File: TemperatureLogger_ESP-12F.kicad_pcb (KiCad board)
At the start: 2 copper layers, 43.7 x 43.7 mm, 19 parts, among them J1 Power for additional devices, J2 Additional I2C device, J3 Barrel_Jack, J4 FTDI, SW1 GND_to_reset, SW2 GND_to_program, U1 ESP-12F, U2 MCP1700-3302E, U6 GY-B11(BME-280)

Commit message: Fixing the programming switch and starting to change the DC jack to fit in the box (component still too high)
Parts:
- J4: value FTDI -> FTDI_Cable
- R7: value 330 -> 100
- SW2: footprint SamacSys_Parts:EG1218 -> TemperatureLogger_ESP-12F:EG1218
- U2: value MCP1700-3302E -> MCP1700-3302E_TO92
- U6: value GY-B11(BME-280) -> GY-B11(BMP-280)
- moved J3 5.51 mm to (142.8, 114.4)
- turned SW2 to 270 degrees
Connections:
- J3 pad 3: (no net) -> Net-(J3-Pad3)
- SW2 pad 2: Earth -> Net-(SW2-Pad2)
- SW2 pad 3: (no net) -> Earth
- U1 pad 10: (no net) -> Net-(U1-Pad10)
- U1 pad 11: (no net) -> Net-(U1-Pad11)
- U1 pad 12: (no net) -> Net-(U1-Pad12)
- U1 pad 13: (no net) -> Net-(U1-Pad13)
- U1 pad 18: Net-(R5-Pad2) -> Net-(SW2-Pad2)
- U1 pad 19: (no net) -> Net-(U1-Pad19)
- U1 pad 2: (no net) -> Net-(U1-Pad2)
- U1 pad 20: (no net) -> Net-(U1-Pad20)
- U1 pad 5: (no net) -> Net-(U1-Pad5)
- U1 pad 7: (no net) -> Net-(U1-Pad7)
- U1 pad 9: (no net) -> Net-(U1-Pad9)
- U6 pad 5: (no net) -> Net-(U6-Pad5)
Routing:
- net Net-(SW2-Pad2): track 0.00 -> 85.0 mm
- net Net-(R5-Pad2): track 87.7 -> 8.82 mm
- net /3.3V: track 160.9 -> 163.9 mm

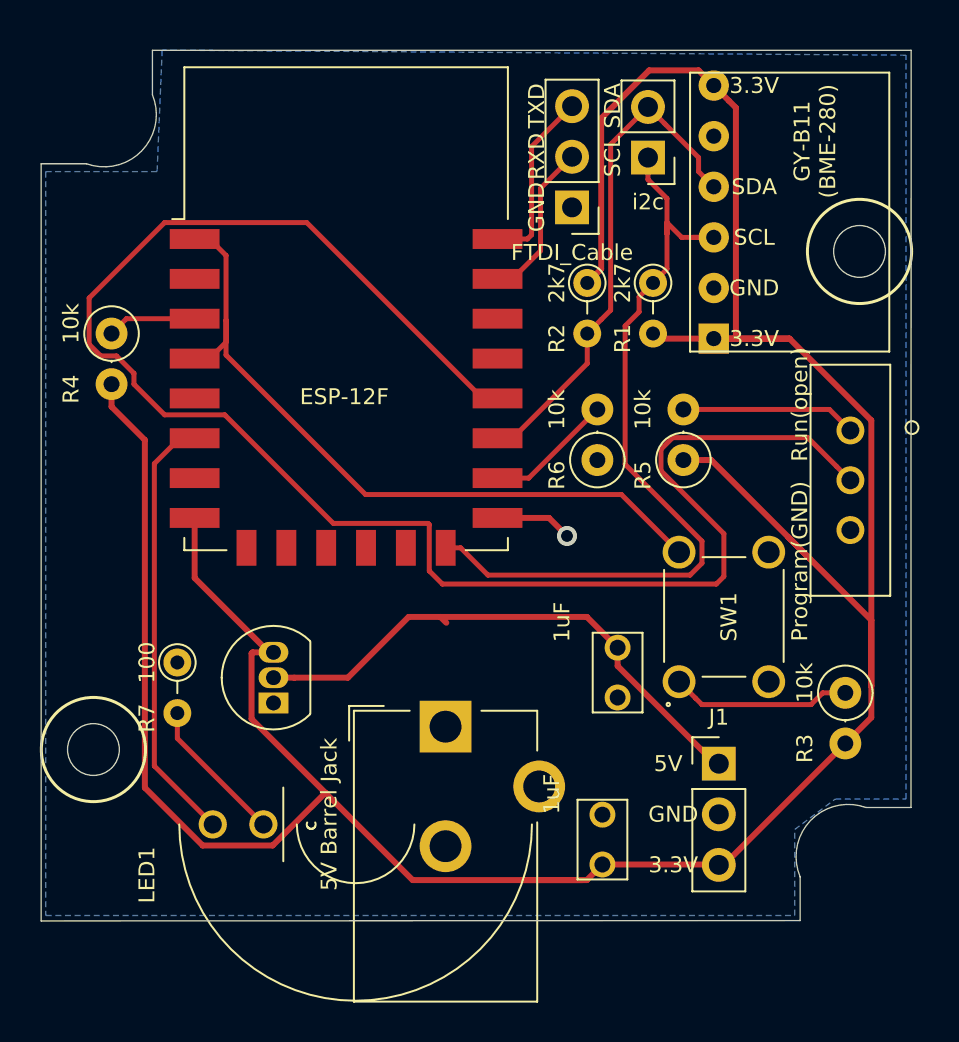
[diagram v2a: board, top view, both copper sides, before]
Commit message: New revisions with headers for power and external sensor
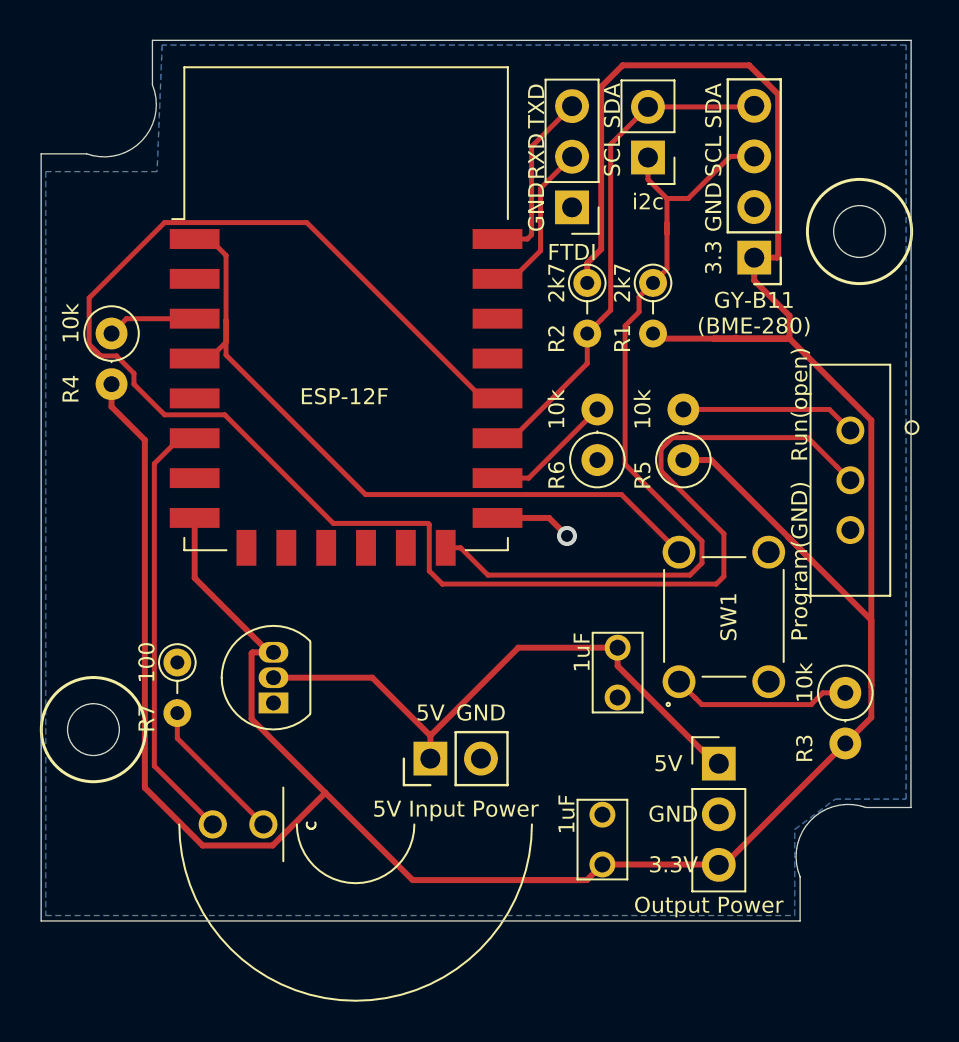
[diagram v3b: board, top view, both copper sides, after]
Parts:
- J3: footprint Connector_BarrelJack:BarrelJack_CUI_PJ-102AH_Horizontal -> Connector_PinHeader_2.54mm:PinHeader_1x02_P2.54mm_Vertical
- J4: value FTDI_Cable -> FTDI
- Output Power: renamed from J1
- U6: footprint ChickmaticPhase3-Simplify:GY-BME280-3.3 -> Connector_PinHeader_2.54mm:PinHeader_1x04_P2.54mm_Vertical
- moved U6 2.90 mm to (158.3, 90.8)
- moved J3 1.78 mm to (142.0, 116.0), turned to 90 degrees
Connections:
- U1 pad 10: Net-(U1-Pad10) -> (no net)
- U1 pad 11: Net-(U1-Pad11) -> (no net)
- U1 pad 12: Net-(U1-Pad12) -> (no net)
- U1 pad 13: Net-(U1-Pad13) -> (no net)
- U1 pad 19: Net-(U1-Pad19) -> (no net)
- U1 pad 2: Net-(U1-Pad2) -> (no net)
- U1 pad 20: Net-(U1-Pad20) -> (no net)
- U1 pad 5: Net-(U1-Pad5) -> (no net)
- U1 pad 7: Net-(U1-Pad7) -> (no net)
- U1 pad 9: Net-(U1-Pad9) -> (no net)
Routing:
- net /3.3V: track 163.9 -> 169.6 mm
- net /5V: track 27.6 -> 29.5 mm
- net /SCL: track 41.2 -> 42.7 mm
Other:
- board size 43.7 x 43.7 mm -> 43.7 x 44.2 mm
- board text added: "+"
- board text added: "3.3"
- board text added: "5V Input Power"
- board text added: "Temperature Logger Cindy Potvin v1.1 https://github.com/CindyPotvin /TemperatureLogger_ESP-12F"
- board text removed: "5V Barrel Jack"

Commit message: Correcting SDA to use GPIO14 instead of pin 14 of ESP8266
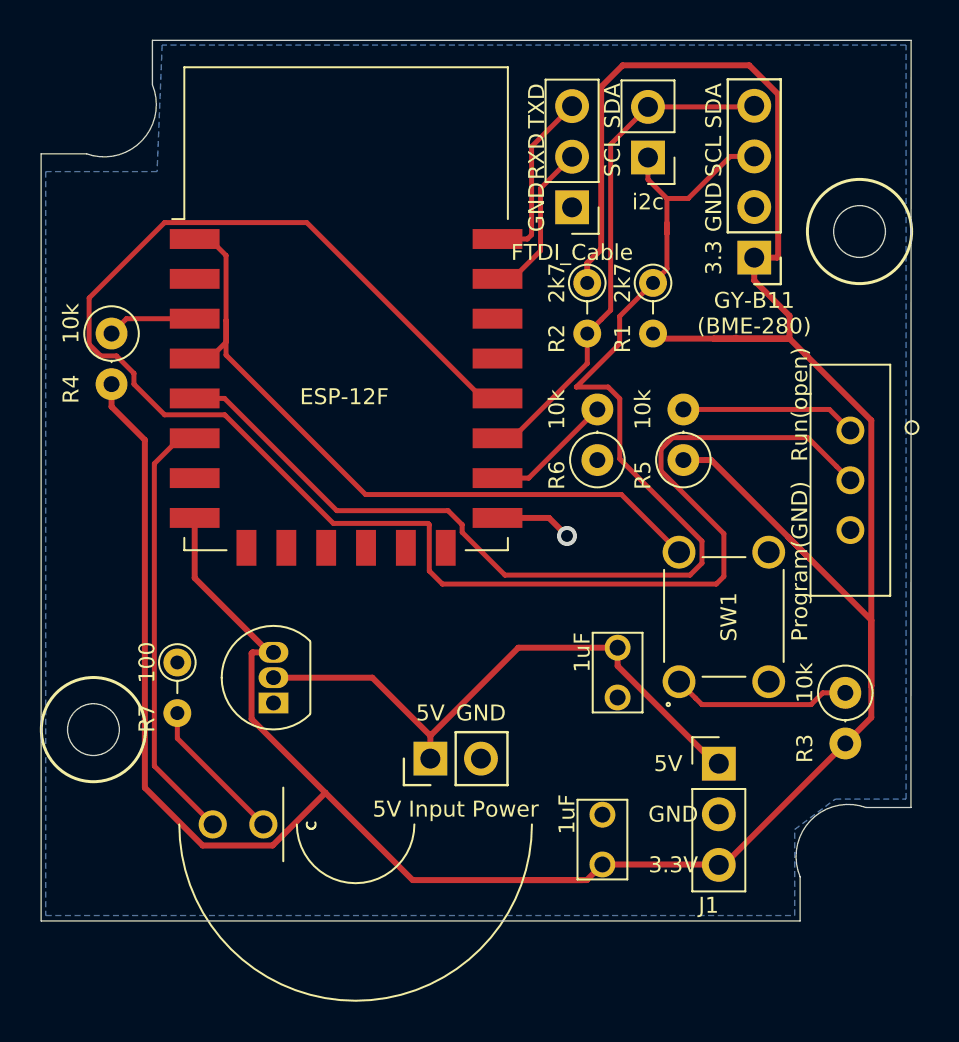
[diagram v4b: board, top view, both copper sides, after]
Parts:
- J1: renamed from Output Power
- J4: value FTDI -> FTDI_Cable
- U2: value MCP1700-3302E_TO92 -> MCP1702-3302E_TO92
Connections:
- U1 pad 14: /SCL -> (no net)
- U1 pad 5: (no net) -> /SCL
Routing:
- net /SCL: track 42.7 -> 61.6 mm
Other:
- board text added: "Temperature Logger Cindy Potvin v1.2 https://github.com/CindyPotvin /TemperatureLogger_ESP-12F"
- board text removed: "Temperature Logger Cindy Potvin v1.1 https://github.com/CindyPotvin /TemperatureLogger_ESP-12F"
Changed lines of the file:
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@@
     (thickness 1.6)
     (drawings 38)
-    (tracks 152)
+    (tracks 158)
     (zones 0)
     (modules 19)
@@
     (pad 15 smd rect (at 7.6 10.5) (size 2.5 1) (layers F.Cu F.Paste F.Mask)
       (net 1 Earth))
-    (pad 14 smd rect (at 5 12) (size 1 1.8) (layers F.Cu F.Paste F.Mask)
-      (net 5 /SCL))
+    (pad 14 smd rect (at 5 12) (size 1 1.8) (layers F.Cu F.Paste F.Mask))
     (pad 13 smd rect (at 3 12) (size 1 1.8) (layers F.Cu F.Paste F.Mask))
     (pad 12 smd rect (at 1 12) (size 1 1.8) (layers F.Cu F.Paste F.Mask))
@@
     (pad 6 smd rect (at -7.6 6.5) (size 2.5 1) (layers F.Cu F.Paste F.Mask)
       (net 14 "Net-(LED1-Pad2)"))
-    (pad 5 smd rect (at -7.6 4.5) (size 2.5 1) (layers F.Cu F.Paste F.Mask))
+    (pad 5 smd rect (at -7.6 4.5) (size 2.5 1) (layers F.Cu F.Paste F.Mask)
+      (net 5 /SCL))
     (pad 4 smd rect (at -7.6 2.5) (size 2.5 1) (layers F.Cu F.Paste F.Mask)
       (net 12 /WAKE))
@@
       (effects (font (size 1 1) (thickness 0.15)))
     )
-    (fp_text value MCP1700-3302E_TO92 (at 2.286 -3.302 90) (layer F.Fab)
+    (fp_text value MCP1702-3302E_TO92 (at 2.286 -3.302 90) (layer F.Fab)
       (effects (font (size 0.8 0.8) (thickness 0.15)))
     )
@@
     (descr "Through hole straight pin header, 1x03, 2.54mm pitch, single row")
     (tags "Through hole pin header THT 1x03 2.54mm single row")
-    (fp_text reference "Output Power" (at -0.508 7.112) (layer F.SilkS)
+    (fp_text reference J1 (at -0.508 7.112) (layer F.SilkS)
       (effects (font (size 0.8 0.8) (thickness 0.15)))
     )
@@
       (effects (font (size 1 1) (thickness 0.15)))
     )
-    (fp_text value FTDI (at 0 -2.268999) (layer F.SilkS)
+    (fp_text value FTDI_Cable (at 0 -2.268999) (layer F.SilkS)
       (effects (font (size 0.8 0.8) (thickness 0.15)))
     )
@@
       (net 1 Earth))
   )
-  (gr_text "Temperature Logger\nCindy Potvin\nv1.1\nhttps://github.com/CindyPotvin\n/TemperatureLogger_ESP-12F" (at 134.631 98.6912 90) (layer B.SilkS)
+  (gr_text "Temperature Logger\nCindy Potvin\nv1.2\nhttps://github.com/CindyPotvin\n/TemperatureLogger_ESP-12F" (at 134.631 98.6912 90) (layer B.SilkS)
     (effects (font (size 1.5 1.5) (thickness 0.3)) (justify mirror))
   )
@@
   (segment (start 158.198 83.2522) (end 158.253 83.1972) (width 0.25) (layer F.Cu) (net 4))
   (segment (start 152.919 83.2522) (end 158.198 83.2522) (width 0.25) (layer F.Cu) (net 4))
-  (segment (start 143.5174 105.3826) (end 142.7674 105.3826) (width 0.25) (layer F.Cu) (net 5))
-  (segment (start 155.031001 106.751201) (end 144.886001 106.751201) (width 0.25) (layer F.Cu) (net 5))
-  (segment (start 144.886001 106.751201) (end 143.5174 105.3826) (width 0.25) (layer F.Cu) (net 5))
-  (segment (start 155.629001 105.049199) (end 155.629001 106.153201) (width 0.25) (layer F.Cu) (net 5))
-  (segment (start 151.771802 101.192) (end 155.629001 105.049199) (width 0.25) (layer F.Cu) (net 5))
-  (segment (start 151.771802 94.2434) (end 151.771802 101.192) (width 0.25) (layer F.Cu) (net 5))
-  (segment (start 155.629001 106.153201) (end 155.031001 106.751201) (width 0.25) (layer F.Cu) (net 5))
-  (segment (start 152.473001 93.542201) (end 151.771802 94.2434) (width 0.25) (layer F.Cu) (net 5))
-  (segment (start 152.473001 92.787199) (end 152.473001 93.542201) (width 0.25) (layer F.Cu) (net 5))
-  (segment (start 153.173 92.0872) (end 152.473001 92.787199) (width 0.25) (layer F.Cu) (net 5))
   (segment (start 153.173 92.0872) (end 153.872999 91.387201) (width 0.25) (layer F.Cu) (net 5))
   (segment (start 153.872999 87.8482) (end 153.872999 89.609201) (width 0.25) (layer F.Cu) (net 5))
@@
   (segment (start 157.050919 85.7372) (end 154.939919 87.8482) (width 0.25) (layer F.Cu) (net 5))
   (segment (start 158.253 85.7372) (end 157.050919 85.7372) (width 0.25) (layer F.Cu) (net 5))
+  (segment (start 155.629001 106.153201) (end 155.031001 106.751201) (width 0.25) (layer F.Cu) (net 5))
+  (segment (start 155.629001 105.049199) (end 155.629001 106.153201) (width 0.25) (layer F.Cu) (net 5))
+  (segment (start 151.504001 100.924199) (end 155.629001 105.049199) (width 0.25) (layer F.Cu) (net 5))
+  (segment (start 151.496019 93.764181) (end 151.496019 95.140391) (width 0.25) (layer F.Cu) (net 5))
+  (segment (start 153.173 92.0872) (end 151.496019 93.764181) (width 0.25) (layer F.Cu) (net 5))
+  (segment (start 151.496019 95.140391) (end 149.324211 97.312199) (width 0.25) (layer F.Cu) (net 5))
+  (segment (start 155.031001 106.751201) (end 145.739001 106.751201) (width 0.25) (layer F.Cu) (net 5))
+  (segment (start 149.324211 97.312199) (end 150.919001 97.312199) (width 0.25) (layer F.Cu) (net 5))
+  (segment (start 150.919001 97.312199) (end 151.504001 97.897199) (width 0.25) (layer F.Cu) (net 5))
+  (segment (start 151.504001 97.897199) (end 151.504001 100.924199) (width 0.25) (layer F.Cu) (net 5))
+  (segment (start 143.592401 104.222599) (end 142.887002 103.5172) (width 0.25) (layer F.Cu) (net 5))
+  (segment (start 145.739001 106.751201) (end 143.592401 104.604601) (width 0.25) (layer F.Cu) (net 5))
+  (segment (start 143.592401 104.604601) (end 143.592401 104.222599) (width 0.25) (layer F.Cu) (net 5))
+  (segment (start 131.6674 97.8826) (end 130.1674 97.8826) (width 0.25) (layer F.Cu) (net 5))
+  (segment (start 137.302 103.5172) (end 131.6674 97.8826) (width 0.25) (layer F.Cu) (net 5))
+  (segment (start 142.887002 103.5172) (end 137.302 103.5172) (width 0.25) (layer F.Cu) (net 5))
   (segment (start 155.303999 112.926199) (end 154.479 112.1012) (width 0.25) (layer F.Cu) (net 6))
   (segment (start 155.629001 113.251201) (end 155.303999 112.926199) (width 0.25) (layer F.Cu) (net 6))
